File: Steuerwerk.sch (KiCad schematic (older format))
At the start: 128 parts, among them J1 2PinTerminalBlocktg, J10 2PinTerminalBlocktg, J11 2PinTerminalBlocktg, J12 2PinTerminalBlocktg, J2 2PinTerminalBlocktg, J3 3PinTerminalBlocktg, J4 3PinTerminalBlocktg, J5 2PinTerminalBlocktg, J6 2PinTerminalBlocktg, J7 2PinTerminalBlocktg, J8 2PinTerminalBlocktg, J9 2PinTerminalBlocktg, Q1 Q_PNP_BCE, U1 74ls240, U2 74541, U3 74LS161, U4 74LS138, U5 74LS138, U6 74541, U7 74LS374, U8 74LS374

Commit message: Verbindungen zum IC fortgeführt
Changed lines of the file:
@@
 L 2PinTerminalBlocktg:2PinTerminalBlocktg J6
 U 1 1 5AC6BD39
-P 2950 7700
-F 0 "J6" V 2766 7765 50  0000 L CNN
-F 1 "2PinTerminalBlocktg" V 2857 7765 50  0000 L CNN
-F 2 "2PinTerminalBlocktg" H 2950 7700 50  0001 L BNN
-F 3 "None" H 2950 7700 50  0001 L BNN
-F 4 "Wurth Electronics" H 2950 7700 50  0001 L BNN "Field4"
-F 5 "None" H 2950 7700 50  0001 L BNN "Field5"
-F 6 "Unavailable" H 2950 7700 50  0001 L BNN "Field6"
-F 7 "TERM BLOCK 2POS HORIZ 5.08MM T/H" H 2950 7700 50  0001 L BNN "Field7"
-F 8 "2PinTerminalBlocktg" H 2950 7700 50  0001 L BNN "Field8"
-	1    2950 7700
-	0    1    1    0
+P 2850 7700
+F 0 "J6" V 2666 7765 50  0000 L CNN
+F 1 "2PinTerminalBlocktg" V 2757 7765 50  0000 L CNN
+F 2 "2PinTerminalBlocktg" H 2850 7700 50  0001 L BNN
+F 3 "None" H 2850 7700 50  0001 L BNN
+F 4 "Wurth Electronics" H 2850 7700 50  0001 L BNN "Field4"
+F 5 "None" H 2850 7700 50  0001 L BNN "Field5"
+F 6 "Unavailable" H 2850 7700 50  0001 L BNN "Field6"
+F 7 "TERM BLOCK 2POS HORIZ 5.08MM T/H" H 2850 7700 50  0001 L BNN "Field7"
+F 8 "2PinTerminalBlocktg" H 2850 7700 50  0001 L BNN "Field8"
+	1    2850 7700
+	0    -1   1    0
 $EndComp
 $Comp
 L 2PinTerminalBlocktg:2PinTerminalBlocktg J7
 U 1 1 5AC6C26F
-P 3500 7700
-F 0 "J7" V 3316 7765 50  0000 L CNN
-F 1 "2PinTerminalBlocktg" V 3407 7765 50  0000 L CNN
-F 2 "2PinTerminalBlocktg" H 3500 7700 50  0001 L BNN
-F 3 "None" H 3500 7700 50  0001 L BNN
-F 4 "Wurth Electronics" H 3500 7700 50  0001 L BNN "Field4"
-F 5 "None" H 3500 7700 50  0001 L BNN "Field5"
-F 6 "Unavailable" H 3500 7700 50  0001 L BNN "Field6"
-F 7 "TERM BLOCK 2POS HORIZ 5.08MM T/H" H 3500 7700 50  0001 L BNN "Field7"
-F 8 "2PinTerminalBlocktg" H 3500 7700 50  0001 L BNN "Field8"
-	1    3500 7700
-	0    1    1    0
+P 3400 7700
+F 0 "J7" V 3216 7765 50  0000 L CNN
+F 1 "2PinTerminalBlocktg" V 3307 7765 50  0000 L CNN
+F 2 "2PinTerminalBlocktg" H 3400 7700 50  0001 L BNN
+F 3 "None" H 3400 7700 50  0001 L BNN
+F 4 "Wurth Electronics" H 3400 7700 50  0001 L BNN "Field4"
+F 5 "None" H 3400 7700 50  0001 L BNN "Field5"
+F 6 "Unavailable" H 3400 7700 50  0001 L BNN "Field6"
+F 7 "TERM BLOCK 2POS HORIZ 5.08MM T/H" H 3400 7700 50  0001 L BNN "Field7"
+F 8 "2PinTerminalBlocktg" H 3400 7700 50  0001 L BNN "Field8"
+	1    3400 7700
+	0    -1   1    0
 $EndComp
 $Comp
 L 2PinTerminalBlocktg:2PinTerminalBlocktg J8
 U 1 1 5AC6C549
-P 4100 7700
-F 0 "J8" V 3916 7765 50  0000 L CNN
-F 1 "2PinTerminalBlocktg" V 4007 7765 50  0000 L CNN
-F 2 "2PinTerminalBlocktg" H 4100 7700 50  0001 L BNN
-F 3 "None" H 4100 7700 50  0001 L BNN
-F 4 "Wurth Electronics" H 4100 7700 50  0001 L BNN "Field4"
-F 5 "None" H 4100 7700 50  0001 L BNN "Field5"
-F 6 "Unavailable" H 4100 7700 50  0001 L BNN "Field6"
-F 7 "TERM BLOCK 2POS HORIZ 5.08MM T/H" H 4100 7700 50  0001 L BNN "Field7"
-F 8 "2PinTerminalBlocktg" H 4100 7700 50  0001 L BNN "Field8"
-	1    4100 7700
-	0    1    1    0
+P 4000 7700
+F 0 "J8" V 3816 7765 50  0000 L CNN
+F 1 "2PinTerminalBlocktg" V 3907 7765 50  0000 L CNN
+F 2 "2PinTerminalBlocktg" H 4000 7700 50  0001 L BNN
+F 3 "None" H 4000 7700 50  0001 L BNN
+F 4 "Wurth Electronics" H 4000 7700 50  0001 L BNN "Field4"
+F 5 "None" H 4000 7700 50  0001 L BNN "Field5"
+F 6 "Unavailable" H 4000 7700 50  0001 L BNN "Field6"
+F 7 "TERM BLOCK 2POS HORIZ 5.08MM T/H" H 4000 7700 50  0001 L BNN "Field7"
+F 8 "2PinTerminalBlocktg" H 4000 7700 50  0001 L BNN "Field8"
+	1    4000 7700
+	0    -1   1    0
 $EndComp
 $Comp
@@
 	3400 7500 3350 7500
 Wire Wire Line
-	3050 7500 2950 7500
-Wire Wire Line
 	2850 7500 2750 7500
 Connection ~ 7800 1350
@@
 Wire Wire Line
 	7550 1000 7550 1150
+Wire Wire Line
+	3050 7500 2950 7500
 $EndSCHEMATC

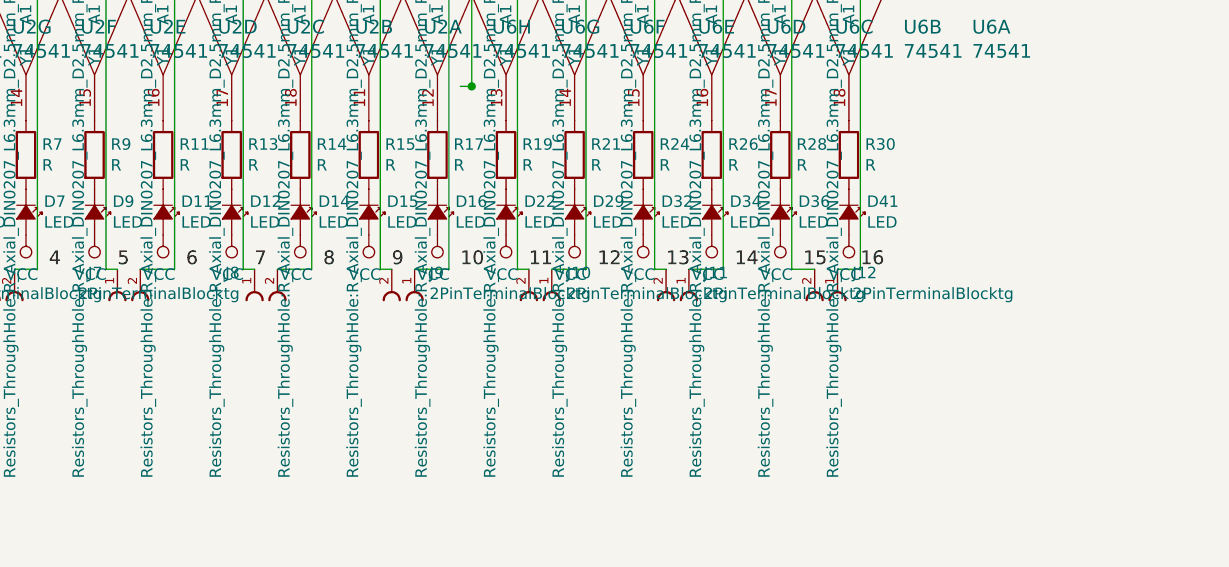
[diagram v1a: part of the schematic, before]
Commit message: Leiterbahnen Korrigiert
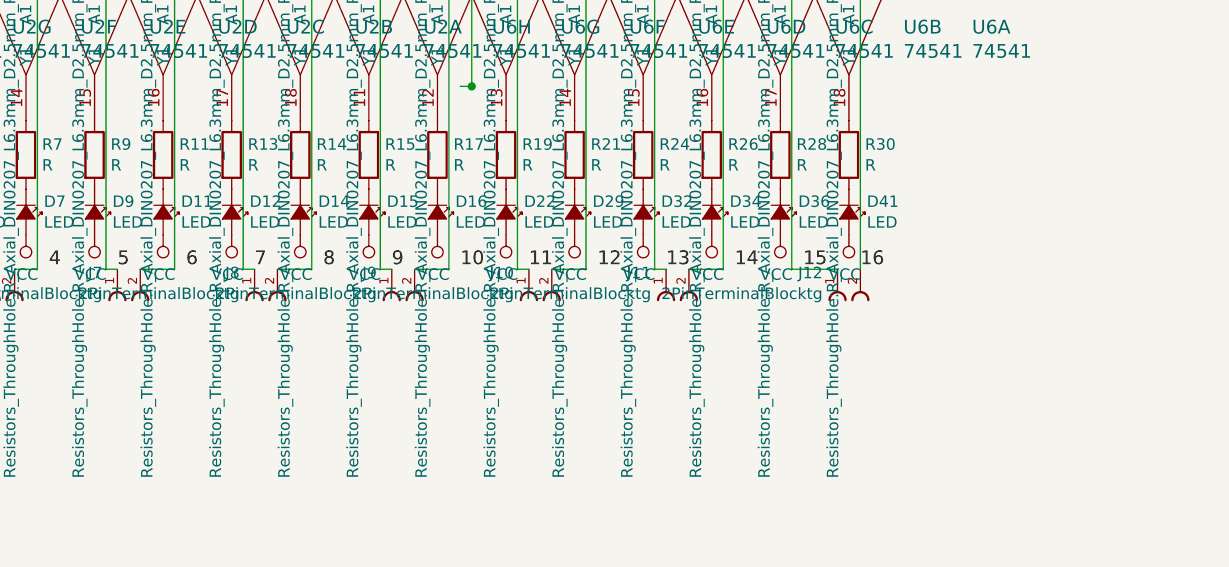
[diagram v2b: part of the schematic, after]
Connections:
- wire segments 442 -> 441
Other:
- moved on the sheet: J12
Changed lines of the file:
@@
 L 2PinTerminalBlocktg:2PinTerminalBlocktg J9
 U 1 1 5AC6C811
-P 4700 7700
-F 0 "J9" V 4516 7765 50  0000 L CNN
-F 1 "2PinTerminalBlocktg" V 4607 7765 50  0000 L CNN
-F 2 "2PinTerminalBlocktg" H 4700 7700 50  0001 L BNN
-F 3 "None" H 4700 7700 50  0001 L BNN
-F 4 "Wurth Electronics" H 4700 7700 50  0001 L BNN "Field4"
-F 5 "None" H 4700 7700 50  0001 L BNN "Field5"
-F 6 "Unavailable" H 4700 7700 50  0001 L BNN "Field6"
-F 7 "TERM BLOCK 2POS HORIZ 5.08MM T/H" H 4700 7700 50  0001 L BNN "Field7"
-F 8 "2PinTerminalBlocktg" H 4700 7700 50  0001 L BNN "Field8"
-	1    4700 7700
-	0    1    1    0
+P 4600 7700
+F 0 "J9" V 4416 7765 50  0000 L CNN
+F 1 "2PinTerminalBlocktg" V 4507 7765 50  0000 L CNN
+F 2 "2PinTerminalBlocktg" H 4600 7700 50  0001 L BNN
+F 3 "None" H 4600 7700 50  0001 L BNN
+F 4 "Wurth Electronics" H 4600 7700 50  0001 L BNN "Field4"
+F 5 "None" H 4600 7700 50  0001 L BNN "Field5"
+F 6 "Unavailable" H 4600 7700 50  0001 L BNN "Field6"
+F 7 "TERM BLOCK 2POS HORIZ 5.08MM T/H" H 4600 7700 50  0001 L BNN "Field7"
+F 8 "2PinTerminalBlocktg" H 4600 7700 50  0001 L BNN "Field8"
+	1    4600 7700
+	0    -1   1    0
 $EndComp
 $Comp
 L 2PinTerminalBlocktg:2PinTerminalBlocktg J10
 U 1 1 5AC6CAD5
-P 5300 7700
-F 0 "J10" V 5116 7765 50  0000 L CNN
-F 1 "2PinTerminalBlocktg" V 5207 7765 50  0000 L CNN
-F 2 "2PinTerminalBlocktg" H 5300 7700 50  0001 L BNN
-F 3 "None" H 5300 7700 50  0001 L BNN
-F 4 "Wurth Electronics" H 5300 7700 50  0001 L BNN "Field4"
-F 5 "None" H 5300 7700 50  0001 L BNN "Field5"
-F 6 "Unavailable" H 5300 7700 50  0001 L BNN "Field6"
-F 7 "TERM BLOCK 2POS HORIZ 5.08MM T/H" H 5300 7700 50  0001 L BNN "Field7"
-F 8 "2PinTerminalBlocktg" H 5300 7700 50  0001 L BNN "Field8"
-	1    5300 7700
-	0    1    1    0
+P 5200 7700
+F 0 "J10" V 5016 7765 50  0000 L CNN
+F 1 "2PinTerminalBlocktg" V 5107 7765 50  0000 L CNN
+F 2 "2PinTerminalBlocktg" H 5200 7700 50  0001 L BNN
+F 3 "None" H 5200 7700 50  0001 L BNN
+F 4 "Wurth Electronics" H 5200 7700 50  0001 L BNN "Field4"
+F 5 "None" H 5200 7700 50  0001 L BNN "Field5"
+F 6 "Unavailable" H 5200 7700 50  0001 L BNN "Field6"
+F 7 "TERM BLOCK 2POS HORIZ 5.08MM T/H" H 5200 7700 50  0001 L BNN "Field7"
+F 8 "2PinTerminalBlocktg" H 5200 7700 50  0001 L BNN "Field8"
+	1    5200 7700
+	0    -1   1    0
 $EndComp
 $Comp
 L 2PinTerminalBlocktg:2PinTerminalBlocktg J11
 U 1 1 5AC6DC3D
-P 5900 7700
-F 0 "J11" V 5716 7765 50  0000 L CNN
-F 1 "2PinTerminalBlocktg" V 5807 7765 50  0000 L CNN
-F 2 "2PinTerminalBlocktg" H 5900 7700 50  0001 L BNN
-F 3 "None" H 5900 7700 50  0001 L BNN
-F 4 "Wurth Electronics" H 5900 7700 50  0001 L BNN "Field4"
-F 5 "None" H 5900 7700 50  0001 L BNN "Field5"
-F 6 "Unavailable" H 5900 7700 50  0001 L BNN "Field6"
-F 7 "TERM BLOCK 2POS HORIZ 5.08MM T/H" H 5900 7700 50  0001 L BNN "Field7"
-F 8 "2PinTerminalBlocktg" H 5900 7700 50  0001 L BNN "Field8"
-	1    5900 7700
-	0    1    1    0
+P 5800 7700
+F 0 "J11" V 5616 7765 50  0000 L CNN
+F 1 "2PinTerminalBlocktg" V 5707 7765 50  0000 L CNN
+F 2 "2PinTerminalBlocktg" H 5800 7700 50  0001 L BNN
+F 3 "None" H 5800 7700 50  0001 L BNN
+F 4 "Wurth Electronics" H 5800 7700 50  0001 L BNN "Field4"
+F 5 "None" H 5800 7700 50  0001 L BNN "Field5"
+F 6 "Unavailable" H 5800 7700 50  0001 L BNN "Field6"
+F 7 "TERM BLOCK 2POS HORIZ 5.08MM T/H" H 5800 7700 50  0001 L BNN "Field7"
+F 8 "2PinTerminalBlocktg" H 5800 7700 50  0001 L BNN "Field8"
+	1    5800 7700
+	0    -1   1    0
 $EndComp
 $Comp
@@
 F 8 "2PinTerminalBlocktg" H 6550 7700 50  0001 L BNN "Field8"
 	1    6550 7700
-	0    1    1    0
-$EndComp
-Wire Wire Line
-	6650 7500 6550 7500
-Wire Wire Line
-	6450 7500 6350 7500
+	0    -1   1    0
+$EndComp
 Wire Wire Line
 	6050 7500 5900 7500
@@
 Wire Wire Line
 	3050 7500 2950 7500
+Wire Wire Line
+	6350 7500 6550 7500
 $EndSCHEMATC

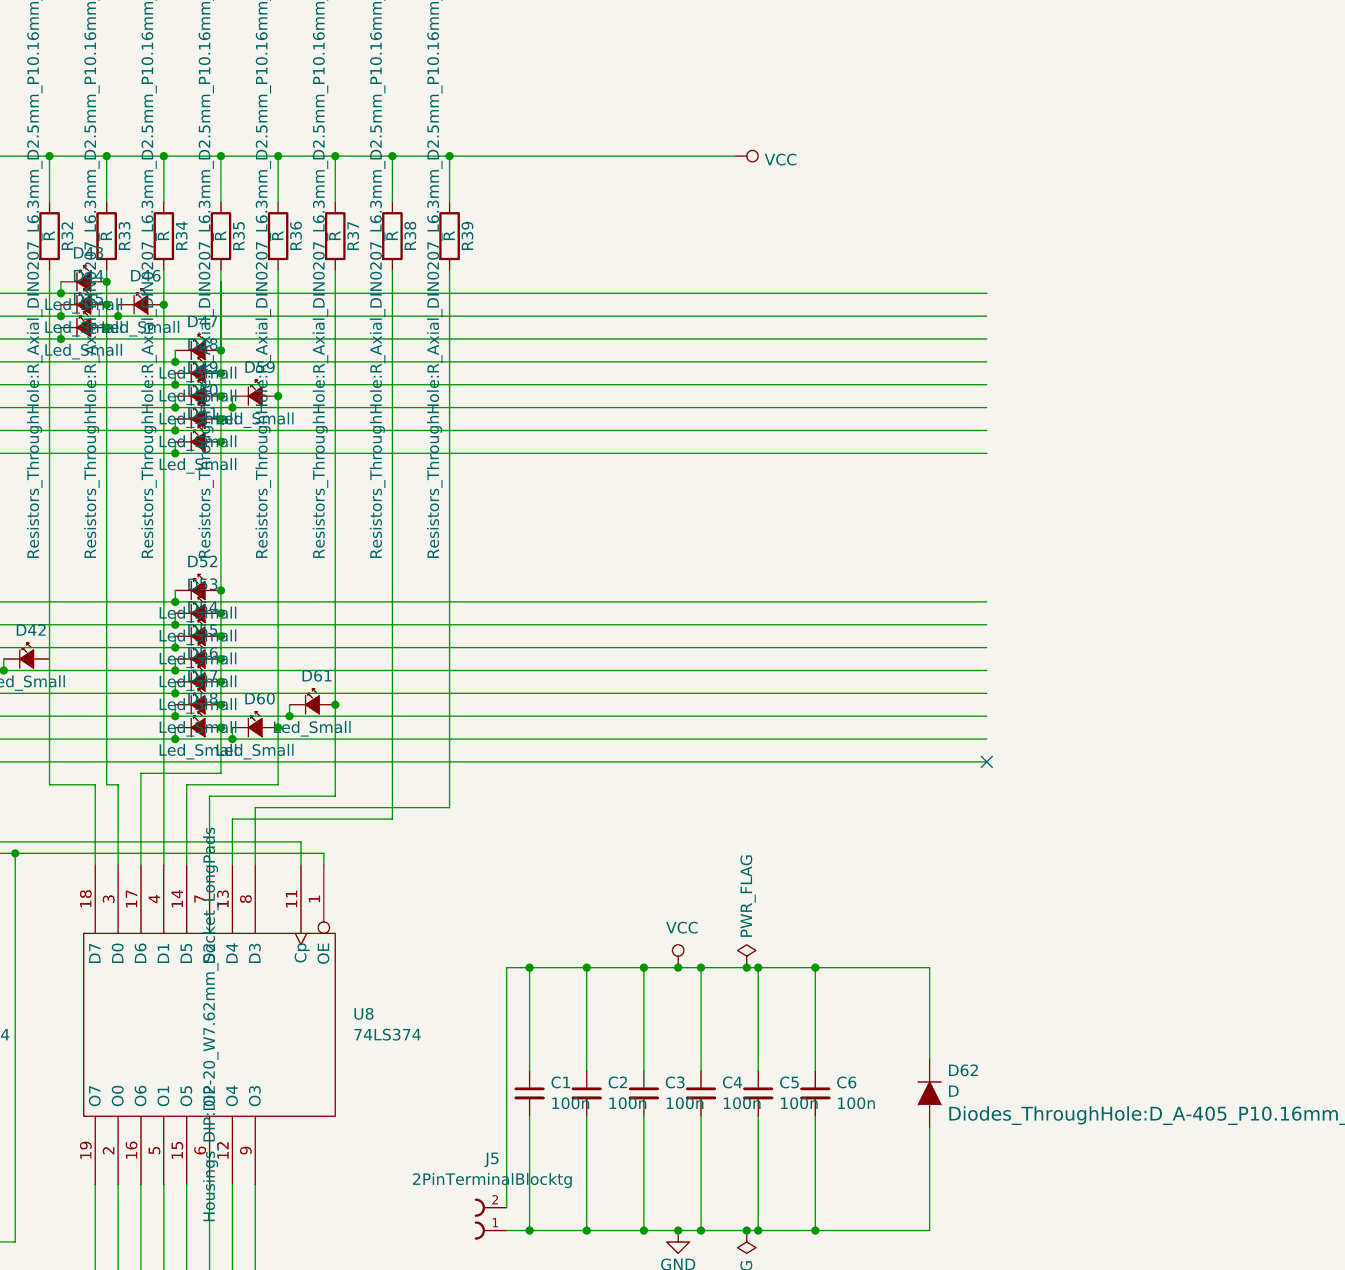
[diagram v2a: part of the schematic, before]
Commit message: falsche ferbindung am lc374 korrigiert und rbussed eingefügt, condensatoren footprinted
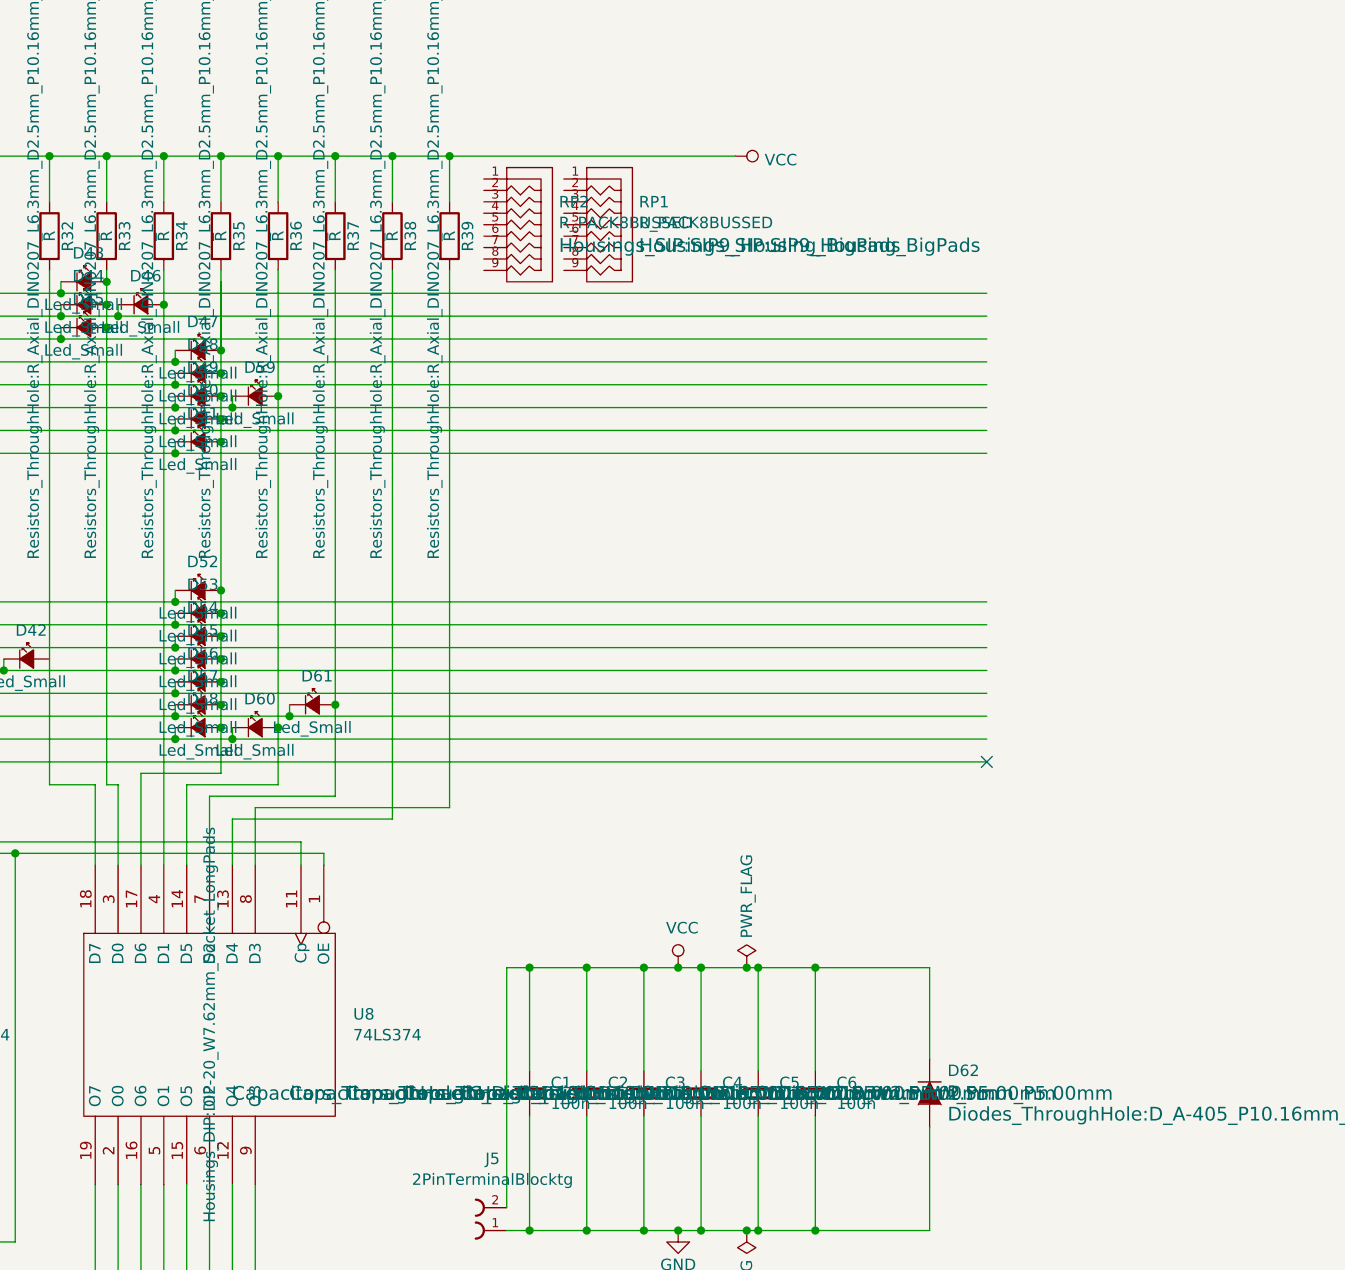
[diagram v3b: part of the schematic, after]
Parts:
- added RP1, RP2: R_PACK8BUSSED, Housings_SIP:SIP9_Housing_BigPads, symbol bonsai:R_PACK8BUSSED
- C1, C2, C3, C4, C5, C6: footprint (none) -> Capacitors_ThroughHole:C_Disc_D10.0mm_W2.5mm_P5.00mm
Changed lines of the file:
@@
 $EndComp
 $Comp
-L 74xx:74LS374 U7
-U 1 1 57E9528C
-P 5950 4300
-F 0 "U7" V 5904 3672 50  0000 R CNN
-F 1 "74LS374" V 5995 3672 50  0000 R CNN
-F 2 "Housings_DIP:DIP-20_W7.62mm_Socket_LongPads" H 5950 4300 50  0001 C CNN
-F 3 "" H 5950 4300 50  0000 C CNN
-	1    5950 4300
-	0    -1   1    0
-$EndComp
-$Comp
 L device:R R4
 U 1 1 57EA1677
@@
 F 0 "C1" H 9242 4646 50  0000 L CNN
 F 1 "100n" H 9242 4555 50  0000 L CNN
-F 2 "" H 9150 4600 60  0000 C CNN
+F 2 "Capacitors_ThroughHole:C_Disc_D10.0mm_W2.5mm_P5.00mm" H 9150 4600 60  0000 C CNN
 F 3 "" H 9150 4600 60  0000 C CNN
 	1    9150 4600
@@
 F 0 "C2" H 9492 4646 50  0000 L CNN
 F 1 "100n" H 9492 4555 50  0000 L CNN
-F 2 "" H 9400 4600 60  0000 C CNN
+F 2 "Capacitors_ThroughHole:C_Disc_D10.0mm_W2.5mm_P5.00mm" H 9400 4600 60  0000 C CNN
 F 3 "" H 9400 4600 60  0000 C CNN
 	1    9400 4600
@@
 F 0 "C3" H 9742 4646 50  0000 L CNN
 F 1 "100n" H 9742 4555 50  0000 L CNN
-F 2 "" H 9650 4600 60  0000 C CNN
+F 2 "Capacitors_ThroughHole:C_Disc_D10.0mm_W2.5mm_P5.00mm" H 9650 4600 60  0000 C CNN
 F 3 "" H 9650 4600 60  0000 C CNN
 	1    9650 4600
@@
 F 0 "C4" H 9992 4646 50  0000 L CNN
 F 1 "100n" H 9992 4555 50  0000 L CNN
-F 2 "" H 9900 4600 60  0000 C CNN
+F 2 "Capacitors_ThroughHole:C_Disc_D10.0mm_W2.5mm_P5.00mm" H 9900 4600 60  0000 C CNN
 F 3 "" H 9900 4600 60  0000 C CNN
 	1    9900 4600
@@
 F 0 "C5" H 10242 4646 50  0000 L CNN
 F 1 "100n" H 10242 4555 50  0000 L CNN
-F 2 "" H 10150 4600 60  0000 C CNN
+F 2 "Capacitors_ThroughHole:C_Disc_D10.0mm_W2.5mm_P5.00mm" H 10150 4600 60  0000 C CNN
 F 3 "" H 10150 4600 60  0000 C CNN
 	1    10150 4600
@@
 F 0 "C6" H 10492 4646 50  0000 L CNN
 F 1 "100n" H 10492 4555 50  0000 L CNN
-F 2 "" H 10400 4600 60  0000 C CNN
+F 2 "Capacitors_ThroughHole:C_Disc_D10.0mm_W2.5mm_P5.00mm" H 10400 4600 60  0000 C CNN
 F 3 "" H 10400 4600 60  0000 C CNN
 	1    10400 4600
@@
 Wire Wire Line
 	6350 7500 6550 7500
+$Comp
+L 74xx:74LS374 U7
+U 1 1 57E9528C
+P 5950 4300
+F 0 "U7" V 5904 3672 50  0000 R CNN
+F 1 "74LS374" V 5995 3672 50  0000 R CNN
+F 2 "Housings_DIP:DIP-20_W7.62mm_Socket_LongPads" H 5950 4300 50  0001 C CNN
+F 3 "" H 5950 4300 50  0000 C CNN
+	1    5950 4300
+	0    -1   1    0
+$EndComp
+$Comp
+L bonsai:R_PACK8BUSSED RP1
+U 1 1 5B1ED72C
+P 9500 800
+F 0 "RP1" H 9628 899 50  0000 L CNN
+F 1 "R_PACK8BUSSED" H 9628 808 50  0000 L CNN
+F 2 "Housings_SIP:SIP9_Housing_BigPads" H 9628 709 60  0000 L CNN
+F 3 "" H 9500 850 60  0000 C CNN
+	1    9500 800
+	1    0    0    -1
+$EndComp
+$Comp
+L bonsai:R_PACK8BUSSED RP2
+U 1 1 5B1EE38D
+P 9150 800
+F 0 "RP2" H 9278 899 50  0000 L CNN
+F 1 "R_PACK8BUSSED" H 9278 808 50  0000 L CNN
+F 2 "Housings_SIP:SIP9_Housing_BigPads" H 9278 709 60  0000 L CNN
+F 3 "" H 9150 850 60  0000 C CNN
+	1    9150 800
+	1    0    0    -1
+$EndComp
 $EndSCHEMATC
